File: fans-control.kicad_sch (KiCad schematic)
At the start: 0 parts

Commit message: WIP Working on fans control circuitry
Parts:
- added C? (x8): C_1u_16V_0402, antmicro-footprints:C_0402_1005Metric, symbol antmicroCapacitors0402:C_1u_16V_0402
- added D? (x4): 1N4148WS-7-F, antmicro-footprints:SOD-323, symbol antmicroDiodesRectifiersSingle:1N4148WS-7-F
- added FB? (x4): FB_120Z_3A_0603, antmicro-footprints:FB_0603_1608Metric, symbol antmicroFerriteBeadsandChips:FB_120Z_3A_0603
- added J? (x4): PinHeader_1x4_P2.5mm_Drill1mm_Horizontal_Shrouded, antmicro-footprints:PinHeader_1x4_P2.5mm_Drill1mm_Horizontal_Shrouded, symbol antmicroRectangularConnectorsHeadersMalePins:PinHeader_1x4_P2.5mm_Drill1mm_Hori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
- added Q?: BSS84PH6327XTSA2, antmicro-footprints:SOT-23-3, symbol antmicroTransistorsFETsMOSFETsSingle:BSS84PH6327XTSA2
- added Q?: 2N7002K-T1-E3, antmicro-footprints:SOT-23-3, symbol antmicroTransistorsFETsMOSFETsSingle:2N7002K-T1-E3
- added R? (x8): R_510k_0402, antmicro-footprints:R_0402_1005Metric, symbol antmicroResistors0402:R_510k_0402
- added U?: LM339_TSSOP, antmicro-footprints:TSSOP-14_4.4x5mm_P0.65mm, symbol antmicroOperationalAmplifiers:LM339_TSSOP
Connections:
- new net: C?.2, R?.2, U?.4
- new net: C?.2, R?.2, U?.6
- new net: C?.2, R?.2, U?.7
- new net: D?.K, FB?.1, J?.2 (x4)
- new net: C?.2, R?.2, U?.9
- new net: C?.2, R?.2, U?.11
- new net: C?.2, R?.2, U?.10
- new net: C?.2, R?.2, U?.5
- new net: C?.2, R?.2, U?.8
- new net 12V0_SYS: FB?.2, FB?.2, FB?.2, FB?.2
- new net FAN_PWM_1: R?.1
- new net FAN_PWM_2: R?.1
- new net FAN_PWM_3: R?.1
- new net FAN_PWM_4: R?.1
- new net FAN_PWM_5: R?.1
- new net FAN_PWM_6: R?.1
- new net FAN_PWM_7: R?.1
- new net FAN_PWM_8: R?.1
- new net FAN_PWM_OUT_1_2: J?.4
- new net FAN_PWM_OUT_3_4: J?.4
- new net FAN_PWM_OUT_5_6: J?.4
- new net FAN_PWM_OUT_7_8: J?.4
- new net FAN_TACH_1_2: J?.3
- new net FAN_TACH_3_4: J?.3
- new net FAN_TACH_5_6: J?.3
- new net FAN_TACH_7_8: J?.3
- new net GND: C?.1, C?.1, C?.1, C?.1, C?.1, C?.1, C?.1, C?.1, D?.A, D?.A, D?.A, D?.A, J?.1, J?.1, J?.1, J?.1, U?.12 (V-)
- new net VCC3V3: U?.3 (V+)
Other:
- note added: "Fans connectors"

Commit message: Cosmetic changes
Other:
- moved on the sheet: C?, D?, FB?, J?, Q?, R?, U?

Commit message: Updated schematic
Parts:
- removed Q?: BSS84PH6327XTSA2, antmicro-footprints:SOT-23-3, symbol antmicroTransistorsFETsMOSFETsSingle:BSS84PH6327XTSA2
- removed Q?: 2N7002K-T1-E3, antmicro-footprints:SOT-23-3, symbol antmicroTransistorsFETsMOSFETsSingle:2N7002K-T1-E3
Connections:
- net VCC3V3 renamed VCC5V0
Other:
- note added: "5V PWM 30Hz signal"
- moved on the sheet: C?, D?, FB?, J?, R?, U?

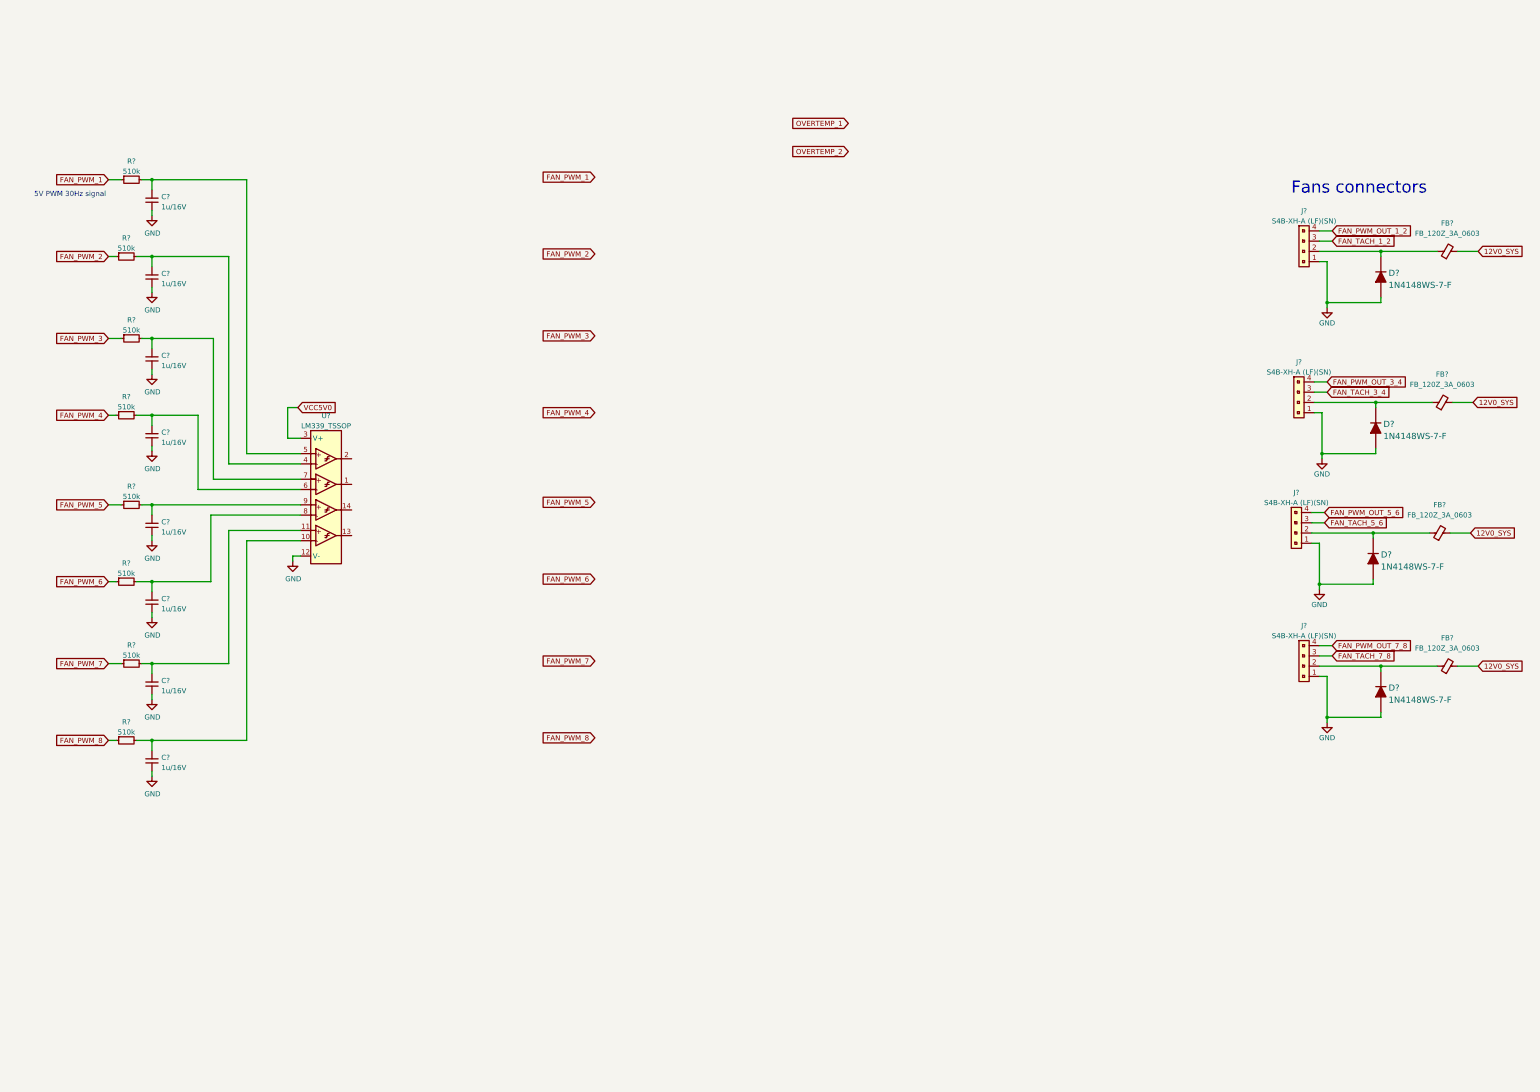
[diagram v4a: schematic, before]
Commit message: Proposed arbiter for controlling fans
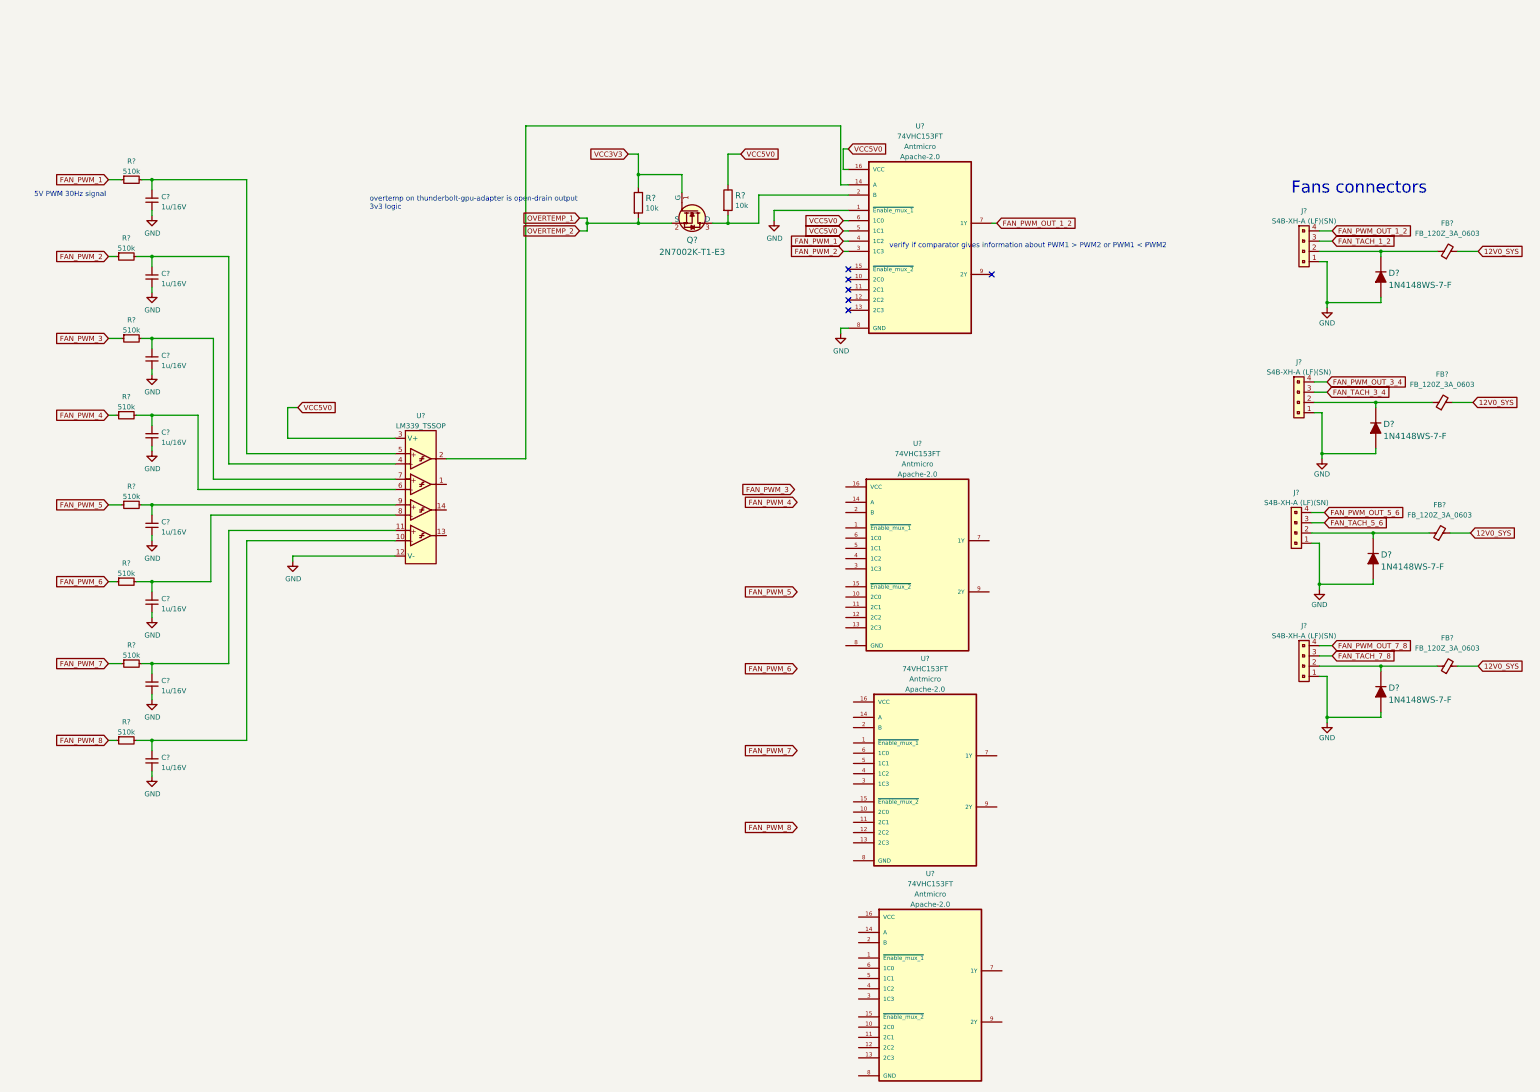
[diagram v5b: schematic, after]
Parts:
- added Q?: 2N7002K-T1-E3, antmicro-footprints:SOT-23-3, symbol antmicroTransistorsFETsMOSFETsSingle:2N7002K-T1-E3
- added R? (x2): R_10k_0402, antmicro-footprints:R_0402_1005Metric, symbol antmicroResistors0402:R_10k_0402
- added U? (x4): 74VHC153FT, antmicro-footprints:TSSOP-16_4.4x5mm_P0.65mm, symbol antmicroInterfaceAnalogSwitchesMultiplexersDemultiplexers:74VHC153FT
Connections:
- net FAN_PWM_1: now also U?.4 (1C2)
- net FAN_PWM_2: now also U?.3 (1C3)
- net FAN_PWM_OUT_1_2: now also U?.7 (1Y)
- net GND: now also U?.1 (~{Enable_mux_1}), U?.8 (GND)
- net OVERTEMP_1: now also Q?.2 (S), R?.2
- net VCC5V0: now also R?.1, U?.16 (VCC), U?.5 (1C1), U?.6 (1C0)
- net at U?.2: now also U?.14 (A)
- new net: Q?.3 (D), R?.2, U?.2 (B)
- new net VCC3V3: Q?.1 (G), R?.1
- no-connect marks 0 -> 6
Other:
- note added: "overtemp on thunderbolt-gpu-adapter is open-drain output 3v3 logic"
- note added: "verify if comparator gives information about PWM1 > PWM2 or PWM1 < PWM2"
- moved on the sheet: U?

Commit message: Rearange hierarchical schematics
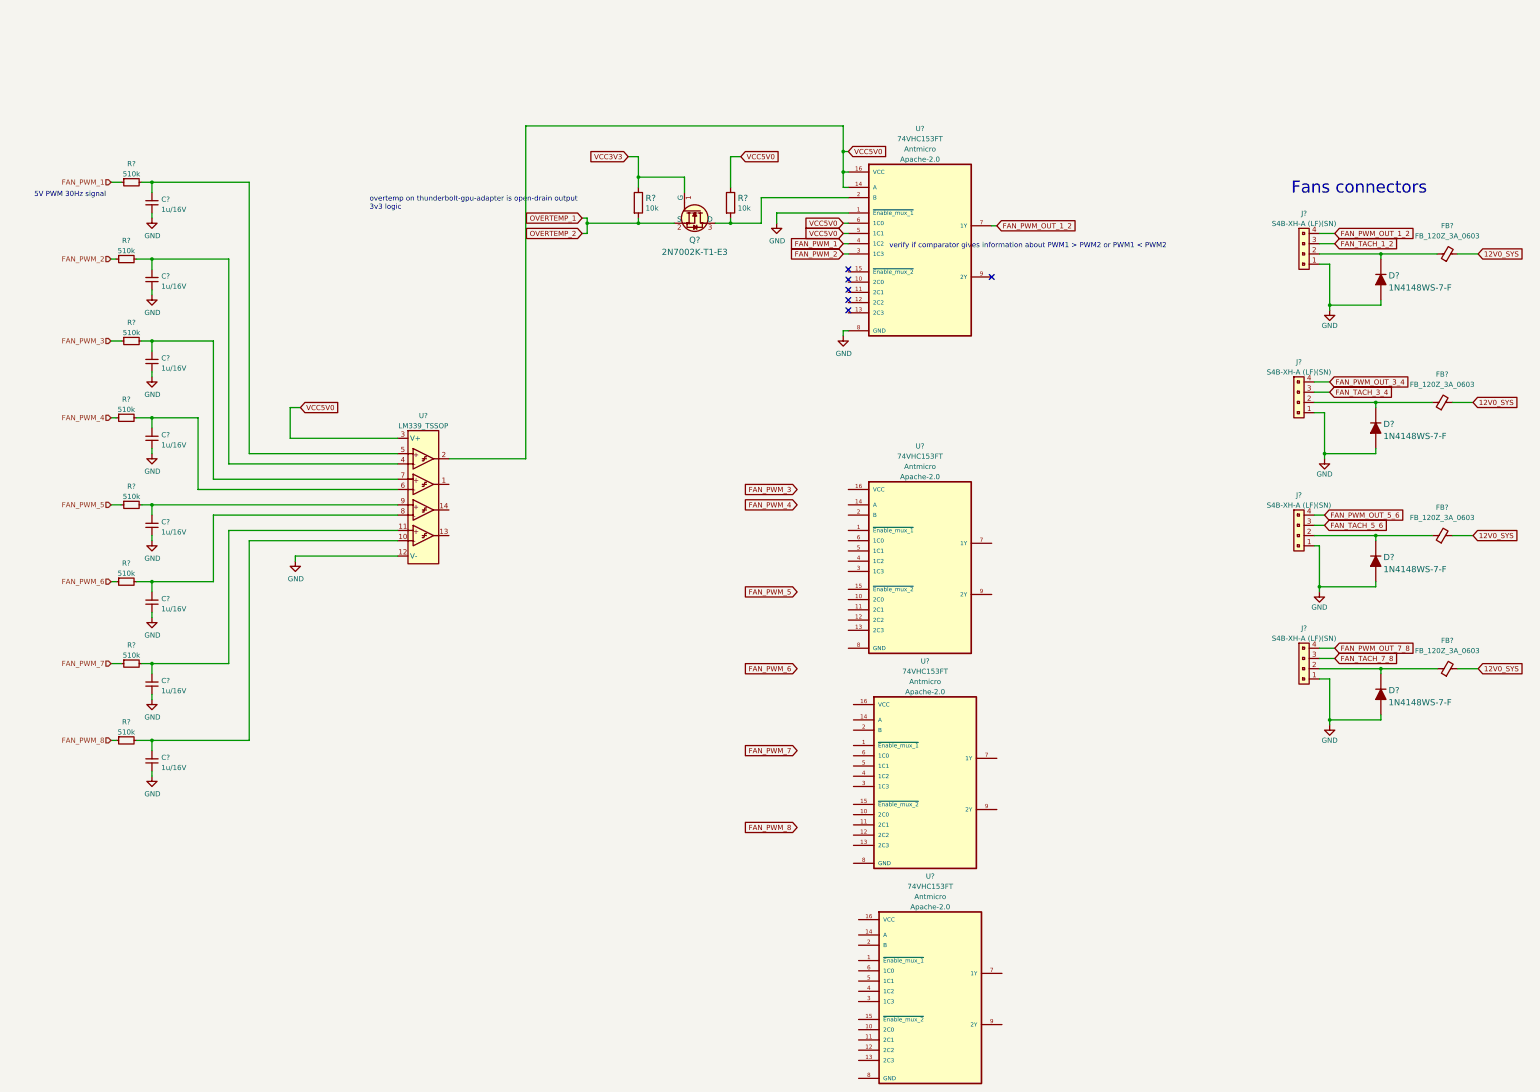
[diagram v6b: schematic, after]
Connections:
- net VCC5V0: now also U?.14 (A), U?.2
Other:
- moved on the sheet: C?, D?, FB?, J?, Q?, R?, U?

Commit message: Mock placement of all components on schematic
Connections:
- net 12V0_SYS renamed VCC12V0
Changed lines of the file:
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@@
-    )
-  )
-  (global_label "12V0_SYS" (shape input) (at 383.54 114.3 0) (fields_autoplaced)
-    (effects (font (size 1.27 1.27)) (justify left))
-    (property "Intersheet References" "${INTERSHEET_REFS}" (id 0) (at 395.1455 114.2206 0)
-      (effects (font (size 1.27 1.27)) (justify left) hide)
-    )
-  )
-  (global_label "12V0_SYS" (shape input) (at 383.54 147.32 0) (fields_autoplaced)
-    (effects (font (size 1.27 1.27)) (justify left))
-    (property "Intersheet References" "${INTERSHEET_REFS}" (id 0) (at 395.1455 147.2406 0)
-      (effects (font (size 1.27 1.27)) (justify left) hide)
     )
   )
@@
     )
   )
-  (global_label "12V0_SYS" (shape input) (at 384.81 77.47 0) (fields_autoplaced)
+  (global_label "VCC12V0" (shape input) (at 384.81 77.47 0) (fields_autoplaced)
     (effects (font (size 1.27 1.27)) (justify left))
-    (property "Intersheet References" "${INTERSHEET_REFS}" (id 0) (at 396.4155 77.3906 0)
+    (property "Intersheet References" "${INTERSHEET_REFS}" (id 0) (at 395.4799 77.5494 0)
       (effects (font (size 1.27 1.27)) (justify left) hide)
     )
@@
     (property "Intersheet References" "${INTERSHEET_REFS}" (id 0) (at 202.7506 161.2106 0)
       (effects (font (size 1.27 1.27)) (justify right) hide)
-    )
-  )
-  (global_label "12V0_SYS" (shape input) (at 384.81 180.34 0) (fields_autoplaced)
-    (effects (font (size 1.27 1.27)) (justify left))
-    (property "Intersheet References" "${INTERSHEET_REFS}" (id 0) (at 396.4155 180.2606 0)
-      (effects (font (size 1.27 1.27)) (justify left) hide)
     )
   )
@@
     )
   )
+  (global_label "VCC12V0" (shape input) (at 383.54 147.32 0) (fields_autoplaced)
+    (effects (font (size 1.27 1.27)) (justify left))
+    (property "Intersheet References" "${INTERSHEET_REFS}" (id 0) (at 394.2099 147.3994 0)
+      (effects (font (size 1.27 1.27)) (justify left) hide)
+    )
+  )
   (global_label "VCC5V0" (shape input) (at 228.6 52.07 0) (fields_autoplaced)
     (effects (font (size 1.27 1.27)) (justify left))
     (property "Intersheet References" "${INTERSHEET_REFS}" (id 0) (at 238.0604 51.9906 0)
+      (effects (font (size 1.27 1.27)) (justify left) hide)
+    )
+  )
+  (global_label "VCC12V0" (shape input) (at 383.54 114.3 0) (fields_autoplaced)
+    (effects (font (size 1.27 1.27)) (justify left))
+    (property "Intersheet References" "${INTERSHEET_REFS}" (id 0) (at 394.2099 114.3794 0)
       (effects (font (size 1.27 1.27)) (justify left) hide)
     )
@@
       (effects (font (size 1.27 1.27)) (justify left) hide)
     )
+  )
+  (global_label "VCC12V0" (shape input) (at 384.81 180.34 0) (fields_autoplaced)
+    (effects (font (size 1.27 1.27)) (justify left))
+    (property "Intersheet References" "${INTERSHEET_REFS}" (id 0) (at 395.4799 180.4194 0)
+      (effects (font (size 1.27 1.27)) (justify left) hide)
+    )

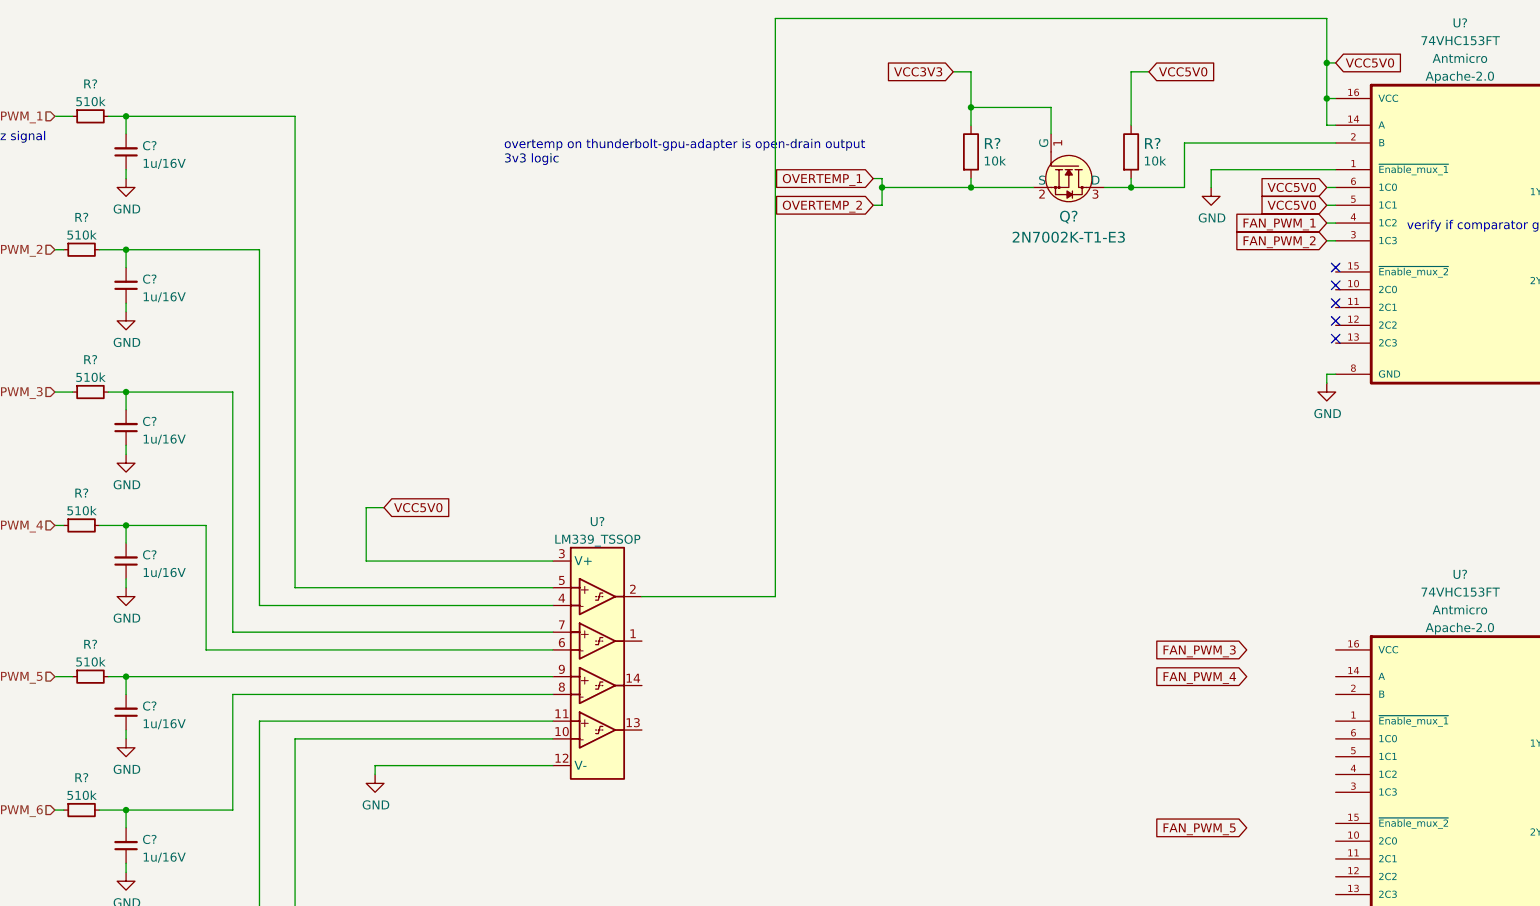
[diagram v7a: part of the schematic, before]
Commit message: Rearrange pwr flags
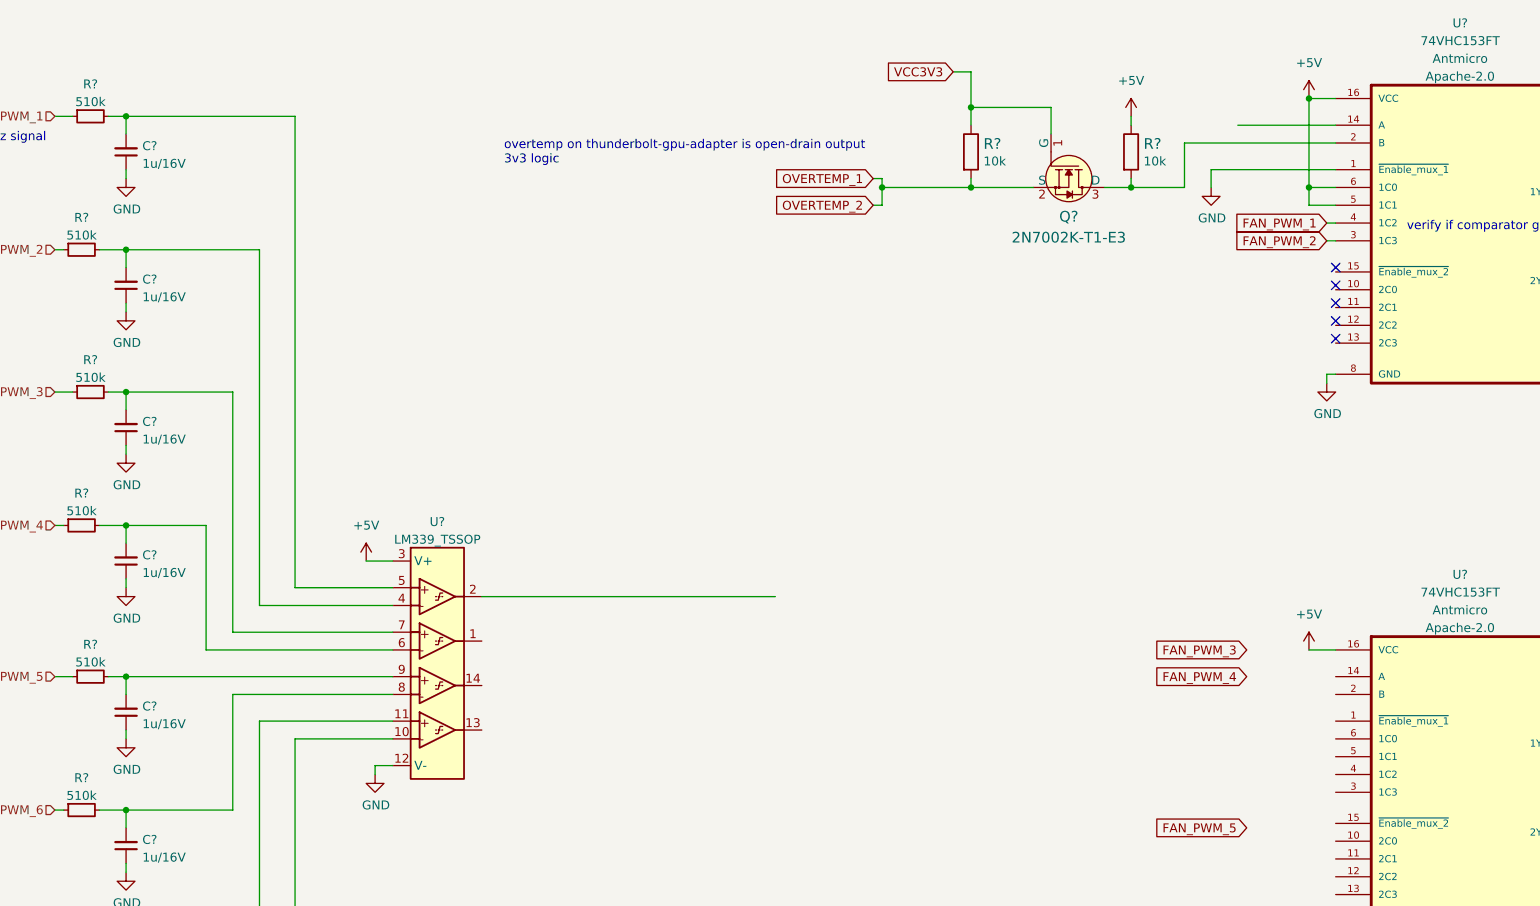
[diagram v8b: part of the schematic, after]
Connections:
- net +5V: now reaches U?.16 (VCC)
- net +5V: now also R?.1, U?.16 (VCC), U?.3 (V+), U?.5 (1C1), U?.6 (1C0)
- removed net VCC5V0: R?.1, U?.14 (A), U?.16 (VCC), U?.2, U?.3 (V+), U?.5 (1C1), U?.6 (1C0)
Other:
- moved on the sheet: U?
